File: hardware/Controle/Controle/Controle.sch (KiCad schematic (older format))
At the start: 11 parts

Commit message: PCB
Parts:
- removed C? (x5): 100n, Capacitor_SMD:C_0805_2012Metric_Pad1.18x1.45mm_HandSolder, symbol Device:C_Small
- removed J?: Conn_01x04, symbol Connector_Generic:Conn_01x04
- removed R?: 4k7, symbol Device:R_Small
- removed U?: STM32F103C8Tx, Package_QFP:LQFP-48_7x7mm_P0.5mm, symbol MCU_ST_STM32F1:STM32F103C8Tx
- removed U?: MCP2551-I-SN, Package_SO:SOIC-8_3.9x4.9mm_P1.27mm, symbol Interface_CAN_LIN:MCP2551-I-SN
- removed U?: AZ1117-5.0, symbol Regulator_Linear:AZ1117-5.0
- removed U?: AZ1117-3.3, symbol Regulator_Linear:AZ1117-3.3
- added C101: 100n, Capacitor_SMD:C_0603_1608Metric_Pad1.08x0.95mm_HandSolder, symbol Device:C_Small
- added D101: LL4148, Diode_SMD:D_SOD-523, symbol Device:D_Small
- added F101: 500ma, Fuse:Fuse_0805_2012Metric_Pad1.15x1.40mm_HandSolder, symbol Device:Fuse
- added J101: USART, Connector_PinHeader_2.54mm:PinHeader_1x04_P2.54mm_Vertical, symbol Connector_Generic:Conn_01x04
- added J102: ST_LINK, Connector_PinHeader_2.54mm:PinHeader_1x04_P2.54mm_Vertical, symbol Connector_Generic:Conn_01x04
- added J103: FAN, Connector_PinHeader_2.54mm:PinHeader_1x02_P2.54mm_Vertical, symbol Connector_Generic:Conn_01x02
- added J104: Switches, Connector_PinHeader_1.27mm:PinHeader_2x07_P1.27mm_Vertical_SMD, symbol Connector_Generic:Conn_02x07_Odd_Even
- added Q101: BCV27, Package_TO_SOT_SMD:SOT-23_Handsoldering, symbol Device:Q_NPN_BEC
- added R101, R102: ?, Resistor_SMD:R_0603_1608Metric_Pad0.98x0.95mm_HandSolder, symbol Device:R_Small
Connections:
- net labels added: +15V, +3V3
- net labels removed: CAN_RX, CAN_TX
- wire segments 59 -> 76

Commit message: adicionado o TL7726 e modificada a placa
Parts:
- J101, J102: footprint Connector_PinHeader_2.54mm:PinHeader_1x04_P2.54mm_Vertical -> Connector_PinHeader_2.54mm:PinHeader_1x04_P2.54mm_Vertical_SMD_Pin1Left
- J103: footprint Connector_PinHeader_2.54mm:PinHeader_1x02_P2.54mm_Vertical -> Connector_PinHeader_2.54mm:PinHeader_1x02_P2.54mm_Vertical_SMD_Pin1Left
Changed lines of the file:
@@
 F 0 "J102" H 1468 2317 50  0000 C CNN
 F 1 "ST_LINK" H 1550 2200 50  0000 C CNN
-F 2 "Connector_PinHeader_2.54mm:PinHeader_1x04_P2.54mm_Vertical" H 1550 2000 50  0001 C CNN
+F 2 "Connector_PinHeader_2.54mm:PinHeader_1x04_P2.54mm_Vertical_SMD_Pin1Left" H 1550 2000 50  0001 C CNN
 F 3 "~" H 1550 2000 50  0001 C CNN
 	1    1550 2000
@@
 F 0 "J101" H 1468 1667 50  0000 C CNN
 F 1 "USART" H 1468 1576 50  0000 C CNN
-F 2 "Connector_PinHeader_2.54mm:PinHeader_1x04_P2.54mm_Vertical" H 1550 1350 50  0001 C CNN
+F 2 "Connector_PinHeader_2.54mm:PinHeader_1x04_P2.54mm_Vertical_SMD_Pin1Left" H 1550 1350 50  0001 C CNN
 F 3 "~" H 1550 1350 50  0001 C CNN
 	1    1550 1350
@@
 F 0 "J103" H 1518 2675 50  0000 C CNN
 F 1 "FAN" H 1600 2800 50  0000 C CNN
-F 2 "Connector_PinHeader_2.54mm:PinHeader_1x02_P2.54mm_Vertical" H 1600 3000 50  0001 C CNN
+F 2 "Connector_PinHeader_2.54mm:PinHeader_1x02_P2.54mm_Vertical_SMD_Pin1Left" H 1600 3000 50  0001 C CNN
 F 3 "~" H 1600 3000 50  0001 C CNN
 	1    1600 3000

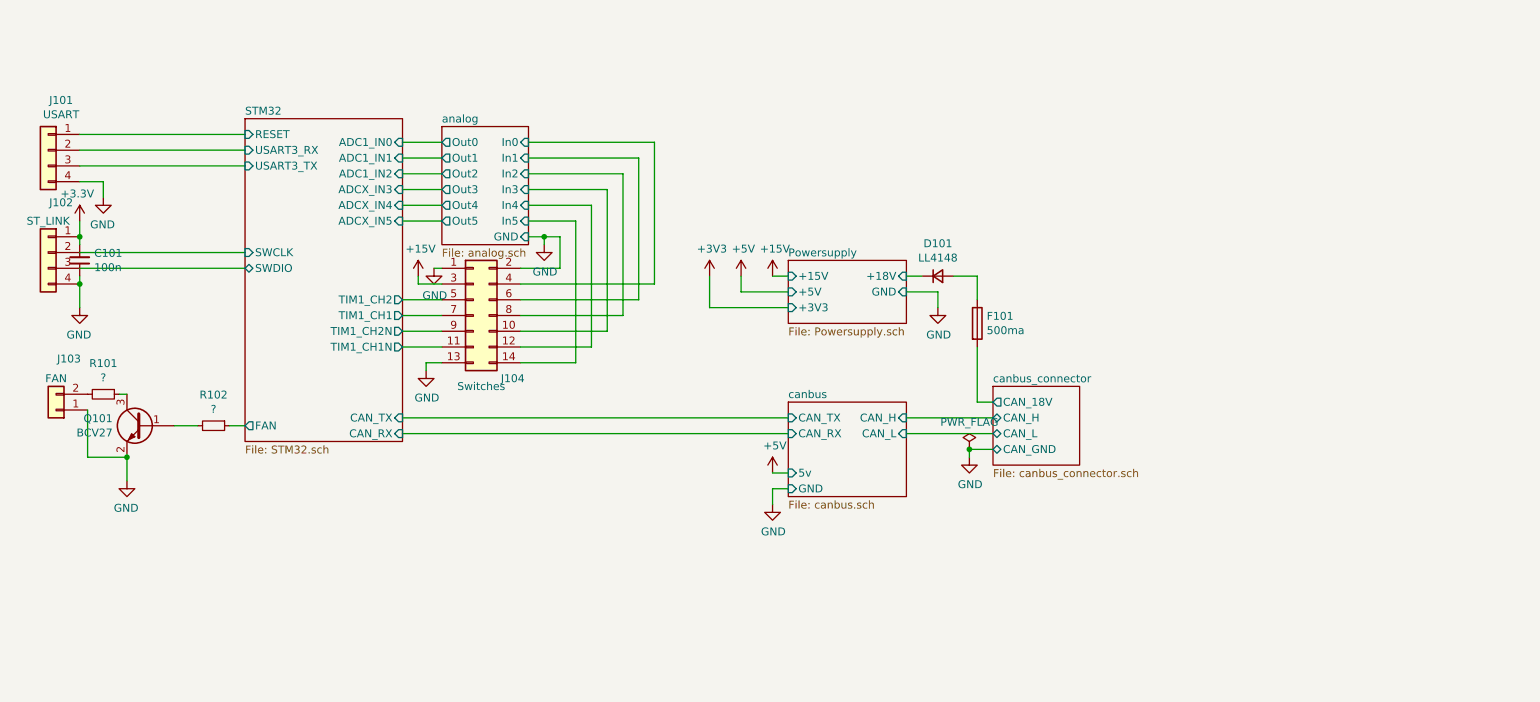
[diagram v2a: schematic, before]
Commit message: control PCB updated
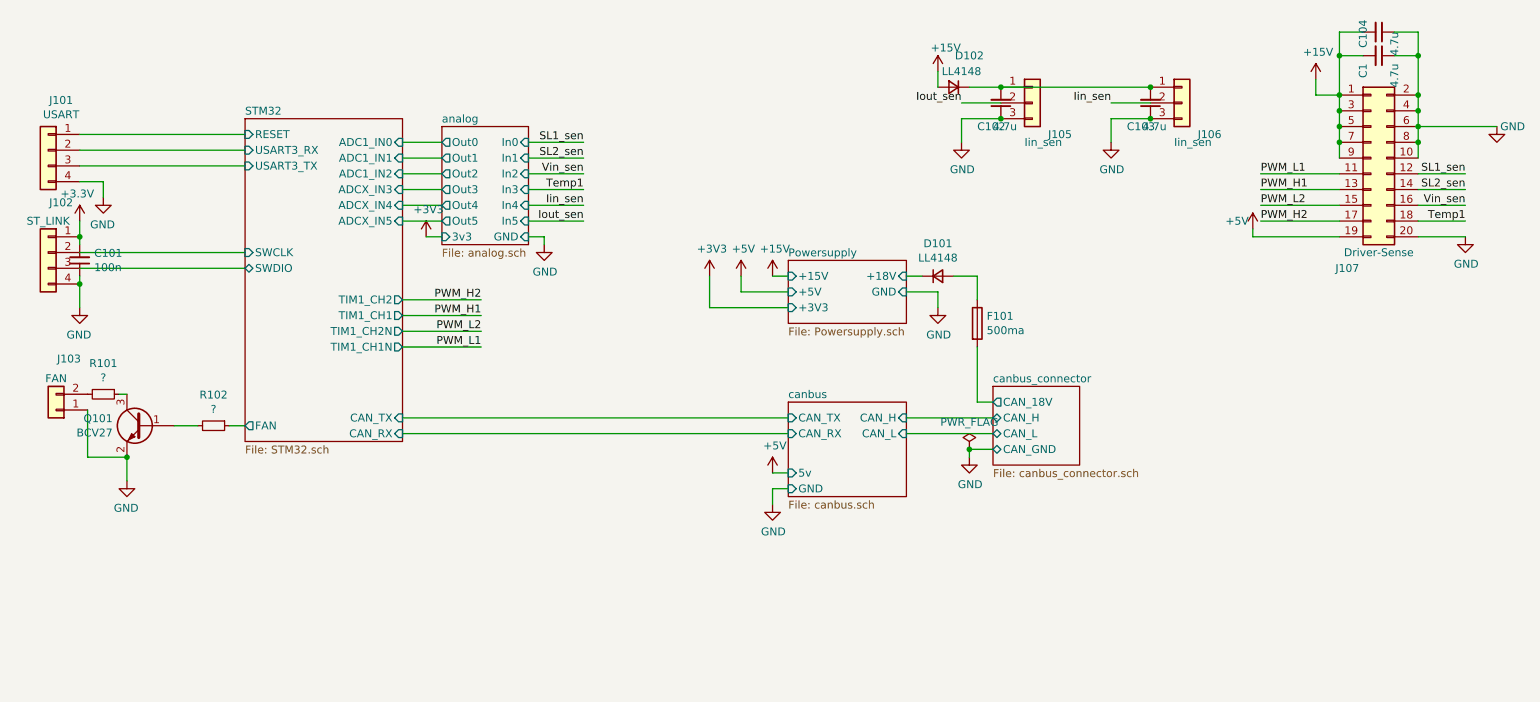
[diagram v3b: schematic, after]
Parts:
- removed J104: Switches, Connector_PinHeader_1.27mm:PinHeader_2x07_P1.27mm_Vertical_SMD, symbol Connector_Generic:Conn_02x07_Odd_Even
- added C1, C102, C103, C104: 4.7u, Capacitor_SMD:C_1210_3225Metric_Pad1.33x2.70mm_HandSolder, symbol Device:C_Small
- added D102: LL4148, Diode_SMD:D_SOD-523, symbol Device:D_Small
- added J105, J106: Iin_sen, Connector_PinHeader_2.54mm:PinHeader_1x03_P2.54mm_Vertical_SMD_Pin1Left, symbol Connector_Generic:Conn_01x03
- added J107: Driver-Sense, KicadZeniteSolarLibrary18:PinSocket_2x10_P1.27mm_Vertical_SMD, symbol Connector_Generic:Conn_02x10_Odd_Even
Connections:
- net +15V: now also C1.2, C104.2, D102.2 (A), J107.1 (Pin_1), J107.3 (Pin_3), J107.5 (Pin_5), J107.7 (Pin_7), J107.9 (Pin_9)
- net +5V: now also J107.19 (Pin_19)
- net GND: now also C1.1, C102.1, C103.1, C104.1, J105.3 (Pin_3), J106.3 (Pin_3), J107.10 (Pin_10), J107.2 (Pin_2), J107.20 (Pin_20), J107.4 (Pin_4), J107.6 (Pin_6), J107.8 (Pin_8)
- new net: C102.2, C103.2, D102.1 (K), J105.1 (Pin_1), J106.1 (Pin_1)
- new net Iin_sen: J106.2 (Pin_2)
- new net Iout_sen: J105.2 (Pin_2)
- new net PWM_H1: J107.13 (Pin_13)
- new net PWM_H2: J107.17 (Pin_17)
- new net PWM_L1: J107.11 (Pin_11)
- new net PWM_L2: J107.15 (Pin_15)
- new net SL1_sen: J107.12 (Pin_12)
- new net SL2_sen: J107.14 (Pin_14)
- new net Temp1: J107.18 (Pin_18)
- new net Vin_sen: J107.16 (Pin_16)

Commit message: Update Controle PCB
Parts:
- D101, D102: value LL4148 -> B0530W; footprint Diode_SMD:D_SOD-523 -> Diode_SMD:D_SOD-123F
- J102: footprint Connector_PinHeader_2.54mm:PinHeader_1x04_P2.54mm_Vertical_SMD_Pin1Left -> Connector_PinHeader_2.54mm:PinHeader_1x05_P2.54mm_Vertical_SMD_Pin1Left; symbol Connector_Generic:Conn_01x04 -> Connector_Generic:Conn_01x05
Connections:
- net GND: now also J102.5 (Pin_5); no longer J102.4 (Pin_4)
- new net STM32/SWO: J102.4 (Pin_4)
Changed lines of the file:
@@
 F18 "SWDIO" B L 2800 2100 50
 F19 "RESET" I L 2800 1250 50
+F20 "SWO" I L 2800 2200 50
 $EndSheet
 $Comp
@@
 Wire Wire Line
 	6150 3400 6250 3400
-$Comp
-L Connector_Generic:Conn_01x04 J102
-U 1 1 6075C4FB
-P 1550 2000
-AR Path="/6075C4FB" Ref="J102"  Part="1"
-AR Path="/607427E0/6075C4FB" Ref="J?"  Part="1"
-F 0 "J102" H 1468 2317 50  0000 C CNN
-F 1 "ST_LINK" H 1550 2200 50  0000 C CNN
-F 2 "Connector_PinHeader_2.54mm:PinHeader_1x04_P2.54mm_Vertical_SMD_Pin1Left" H 1550 2000 50  0001 C CNN
-F 3 "~" H 1550 2000 50  0001 C CNN
-	1    1550 2000
-	-1   0    0    -1
-$EndComp
 $Comp
 L power:GND #PWR0102
@@
 $EndComp
 Wire Wire Line
-	1750 1800 1750 1900
-$Comp
-L Device:C_Small C101
-U 1 1 6075C510
-P 1750 2050
-AR Path="/6075C510" Ref="C101"  Part="1"
-AR Path="/607427E0/6075C510" Ref="C?"  Part="1"
-F 0 "C101" H 1658 2004 50  0000 R CNN
-F 1 "100n" H 1658 2095 50  0000 R CNN
-F 2 "Capacitor_SMD:C_0603_1608Metric_Pad1.08x0.95mm_HandSolder" H 1750 2050 50  0001 C CNN
-F 3 "~" H 1750 2050 50  0001 C CNN
-	1    1750 2050
-	-1   0    0    1
-$EndComp
-Wire Wire Line
-	1750 1950 1750 1900
-Connection ~ 1750 1900
-Wire Wire Line
-	1750 2150 1750 2200
-Connection ~ 1750 2200
-Wire Wire Line
-	1750 2200 1750 2350
-Wire Wire Line
-	1750 2000 2800 2000
-Wire Wire Line
-	1750 2100 2800 2100
+	1700 2100 2800 2100
 $Comp
 L Connector_Generic:Conn_01x04 J101
@@
 Wire Wire Line
 	7450 2300 7450 2150
-$Comp
-L Device:D_Small D101
-U 1 1 6093366B
-P 7200 2150
-F 0 "D101" H 7200 2357 50  0000 C CNN
-F 1 "LL4148" H 7200 2266 50  0000 C CNN
-F 2 "Diode_SMD:D_SOD-523" V 7200 2150 50  0001 C CNN
-F 3 "~" V 7200 2150 50  0001 C CNN
-	1    7200 2150
-	1    0    0    -1
-$EndComp
 Wire Wire Line
 	7100 2150 7000 2150
@@
 P 7300 950
 F 0 "D102" H 7200 750 50  0000 C CNN
-F 1 "LL4148" H 7250 850 50  0000 C CNN
-F 2 "Diode_SMD:D_SOD-523" V 7300 950 50  0001 C CNN
+F 1 "B0530W" H 7050 850 50  0000 C CNN
+F 2 "Diode_SMD:D_SOD-123F" V 7300 950 50  0001 C CNN
 F 3 "~" V 7300 950 50  0001 C CNN
 	1    7300 950
@@
 Wire Wire Line
 	3950 1900 4050 1900
+$Comp
+L Connector_Generic:Conn_01x05 J102
+U 1 1 6075C4FB
+P 1500 2100
+AR Path="/6075C4FB" Ref="J102"  Part="1"
+AR Path="/607427E0/6075C4FB" Ref="J?"  Part="1"
+F 0 "J102" H 1418 2417 50  0000 C CNN
+F 1 "ST_LINK" H 1500 2300 50  0000 C CNN
+F 2 "Connector_PinHeader_2.54mm:PinHeader_1x05_P2.54mm_Vertical_SMD_Pin1Left" H 1500 2100 50  0001 C CNN
+F 3 "~" H 1500 2100 50  0001 C CNN
+	1    1500 2100
+	-1   0    0    -1
+$EndComp
+Wire Wire Line
+	1750 1800 1750 1900
+Wire Wire Line
+	1700 1900 1750 1900
+Connection ~ 1750 1900
+Wire Wire Line
+	1750 2350 1750 2300
+Wire Wire Line
+	1700 2300 1750 2300
+Connection ~ 1750 2300
+Wire Wire Line
+	1750 1900 1750 1950
+Wire Wire Line
+	1700 2000 2800 2000
+Wire Wire Line
+	1750 2300 1750 2150
+Wire Wire Line
+	2800 2200 1700 2200
+$Comp
+L Device:C_Small C101
+U 1 1 6075C510
+P 1750 2050
+AR Path="/6075C510" Ref="C101"  Part="1"
+AR Path="/607427E0/6075C510" Ref="C?"  Part="1"
+F 0 "C101" H 1658 2004 50  0000 R CNN
+F 1 "100n" H 1658 2095 50  0000 R CNN
+F 2 "Capacitor_SMD:C_0603_1608Metric_Pad1.08x0.95mm_HandSolder" H 1750 2050 50  0001 C CNN
+F 3 "~" H 1750 2050 50  0001 C CNN
+	1    1750 2050
+	-1   0    0    1
+$EndComp
+$Comp
+L Device:D_Small D101
+U 1 1 609E3BEA
+P 7200 2150
+F 0 "D101" H 7100 2350 50  0000 C CNN
+F 1 "B0530W" H 7350 2250 50  0000 C CNN
+F 2 "Diode_SMD:D_SOD-123F" V 7200 2150 50  0001 C CNN
+F 3 "~" V 7200 2150 50  0001 C CNN
+	1    7200 2150
+	1    0    0    -1
+$EndComp
 $EndSCHEMATC

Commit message: first version of layout
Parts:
- added H101, H102, H103: MountingHole, MountingHole:MountingHole_3.2mm_M3, symbol Mechanical:MountingHole
- added R103: ?, Resistor_SMD:R_0603_1608Metric_Pad0.98x0.95mm_HandSolder, symbol Device:R_Small
- F101: value 500ma -> 1A; footprint Fuse:Fuse_0805_2012Metric_Pad1.15x1.40mm_HandSolder -> Fuse:Fuse_1812_4532Metric_Pad1.30x3.40mm_HandSolder
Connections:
- net +5V: now also R103.2
- net at J103.2 (Pin_2), R101.2: now also R103.1
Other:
- moved on the sheet: R101
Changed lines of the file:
@@
 L Device:R_Small R101
 U 1 1 60904DF2
-P 1900 2900
-F 0 "R101" V 1704 2900 50  0000 C CNN
-F 1 "?" V 1795 2900 50  0000 C CNN
-F 2 "Resistor_SMD:R_0603_1608Metric_Pad0.98x0.95mm_HandSolder" H 1900 2900 50  0001 C CNN
-F 3 "~" H 1900 2900 50  0001 C CNN
-	1    1900 2900
+P 1950 2900
+F 0 "R101" V 1754 2900 50  0000 C CNN
+F 1 "?" V 1845 2900 50  0000 C CNN
+F 2 "Resistor_SMD:R_0603_1608Metric_Pad0.98x0.95mm_HandSolder" H 1950 2900 50  0001 C CNN
+F 3 "~" H 1950 2900 50  0001 C CNN
+	1    1950 2900
 	0    1    1    0
 $EndComp
-Wire Wire Line
-	2000 2900 2050 2900
 $Comp
 L Device:Fuse F101
@@
 P 7450 2450
 F 0 "F101" H 7510 2496 50  0000 L CNN
-F 1 "500ma" H 7510 2405 50  0000 L CNN
-F 2 "Fuse:Fuse_0805_2012Metric_Pad1.15x1.40mm_HandSolder" V 7380 2450 50  0001 C CNN
+F 1 "1A" H 7510 2405 50  0000 L CNN
+F 2 "Fuse:Fuse_1812_4532Metric_Pad1.30x3.40mm_HandSolder" V 7380 2450 50  0001 C CNN
 F 3 "~" H 7450 2450 50  0001 C CNN
 	1    7450 2450
@@
 	1    0    0    -1
 $EndComp
+$Comp
+L Device:R_Small R103
+U 1 1 60A35BB8
+P 1850 2750
+F 0 "R103" H 1800 2600 50  0000 C CNN
+F 1 "?" H 1650 2600 50  0000 C CNN
+F 2 "Resistor_SMD:R_0603_1608Metric_Pad0.98x0.95mm_HandSolder" H 1850 2750 50  0001 C CNN
+F 3 "~" H 1850 2750 50  0001 C CNN
+	1    1850 2750
+	-1   0    0    1
+$EndComp
+Wire Wire Line
+	1800 2900 1850 2900
+Wire Wire Line
+	1850 2850 1850 2900
+Connection ~ 1850 2900
+$Comp
+L power:+5V #PWR0130
+U 1 1 60A3FB9E
+P 1850 2600
+F 0 "#PWR0130" H 1850 2450 50  0001 C CNN
+F 1 "+5V" H 1865 2773 50  0000 C CNN
+F 2 "" H 1850 2600 50  0001 C CNN
+F 3 "" H 1850 2600 50  0001 C CNN
+	1    1850 2600
+	1    0    0    -1
+$EndComp
+Wire Wire Line
+	1850 2600 1850 2650
+$Comp
+L Mechanical:MountingHole H101
+U 1 1 60AAC1BB
+P 9600 2800
+F 0 "H101" H 9700 2846 50  0000 L CNN
+F 1 "MountingHole" H 9700 2755 50  0000 L CNN
+F 2 "MountingHole:MountingHole_3.2mm_M3" H 9600 2800 50  0001 C CNN
+F 3 "~" H 9600 2800 50  0001 C CNN
+	1    9600 2800
+	1    0    0    -1
+$EndComp
+$Comp
+L Mechanical:MountingHole H102
+U 1 1 60AADB74
+P 9600 3050
+F 0 "H102" H 9700 3096 50  0000 L CNN
+F 1 "MountingHole" H 9700 3005 50  0000 L CNN
+F 2 "MountingHole:MountingHole_3.2mm_M3" H 9600 3050 50  0001 C CNN
+F 3 "~" H 9600 3050 50  0001 C CNN
+	1    9600 3050
+	1    0    0    -1
+$EndComp
+$Comp
+L Mechanical:MountingHole H103
+U 1 1 60AAE00A
+P 9600 3350
+F 0 "H103" H 9700 3396 50  0000 L CNN
+F 1 "MountingHole" H 9700 3305 50  0000 L CNN
+F 2 "MountingHole:MountingHole_3.2mm_M3" H 9600 3350 50  0001 C CNN
+F 3 "~" H 9600 3350 50  0001 C CNN
+	1    9600 3350
+	1    0    0    -1
+$EndComp

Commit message: falta acabamento
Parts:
- added H?: MountingHole, MountingHole:MountingHole_3.2mm_M3, symbol Mechanical:MountingHole
- C1, C102, C103, C104: footprint Capacitor_SMD:C_1210_3225Metric_Pad1.33x2.70mm_HandSolder -> Capacitor_SMD:C_1206_3216Metric_Pad1.33x1.80mm_HandSolder
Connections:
- net STM32/SWCLK: now also J102.4 (Pin_4); no longer J102.2 (Pin_2)
- net STM32/SWDIO: now also J102.2 (Pin_2); no longer J102.3 (Pin_3)
- net STM32/SWO: now also J102.3 (Pin_3); no longer J102.4 (Pin_4)
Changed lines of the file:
@@
 F15 "TIM1_CH1" O R 3800 2400 50
 F16 "TIM1_CH2" O R 3800 2300 50
-F17 "SWCLK" I L 2800 2000 50
-F18 "SWDIO" B L 2800 2100 50
+F17 "SWCLK" I L 2800 2200 50
+F18 "SWDIO" B L 2800 2000 50
 F19 "RESET" I L 2800 1250 50
-F20 "SWO" I L 2800 2200 50
+F20 "SWO" I L 2800 2100 50
 $EndSheet
 $Comp
@@
 F 0 "C1" H 9950 650 50  0000 R CNN
 F 1 "4.7u" H 9950 850 50  0000 R CNN
-F 2 "Capacitor_SMD:C_1210_3225Metric_Pad1.33x2.70mm_HandSolder" H 10000 750 50  0001 C CNN
+F 2 "Capacitor_SMD:C_1206_3216Metric_Pad1.33x1.80mm_HandSolder" H 10000 750 50  0001 C CNN
 F 3 "~" H 10000 750 50  0001 C CNN
 	1    10000 750
@@
 F 0 "C103" H 8700 1200 50  0000 R CNN
 F 1 "4.7u" H 8600 1200 50  0000 R CNN
-F 2 "Capacitor_SMD:C_1210_3225Metric_Pad1.33x2.70mm_HandSolder" H 8550 1050 50  0001 C CNN
+F 2 "Capacitor_SMD:C_1206_3216Metric_Pad1.33x1.80mm_HandSolder" H 8550 1050 50  0001 C CNN
 F 3 "~" H 8550 1050 50  0001 C CNN
 	1    8550 1050
@@
 F 0 "C104" H 10100 500 50  0000 R CNN
 F 1 "4.7u" H 10150 700 50  0000 R CNN
-F 2 "Capacitor_SMD:C_1210_3225Metric_Pad1.33x2.70mm_HandSolder" H 10000 600 50  0001 C CNN
+F 2 "Capacitor_SMD:C_1206_3216Metric_Pad1.33x1.80mm_HandSolder" H 10000 600 50  0001 C CNN
 F 3 "~" H 10000 600 50  0001 C CNN
 	1    10000 600
@@
 F 0 "C102" H 7750 1200 50  0000 R CNN
 F 1 "4.7u" H 7650 1200 50  0000 R CNN
-F 2 "Capacitor_SMD:C_1210_3225Metric_Pad1.33x2.70mm_HandSolder" H 7600 1050 50  0001 C CNN
+F 2 "Capacitor_SMD:C_1206_3216Metric_Pad1.33x1.80mm_HandSolder" H 7600 1050 50  0001 C CNN
 F 3 "~" H 7600 1050 50  0001 C CNN
 	1    7600 1050
@@
 	1    0    0    -1
 $EndComp
+$Comp
+L Mechanical:MountingHole H?
+U 1 1 60B88A3F
+P 9600 3650
+F 0 "H?" H 9700 3696 50  0000 L CNN
+F 1 "MountingHole" H 9700 3605 50  0000 L CNN
+F 2 "MountingHole:MountingHole_3.2mm_M3" H 9600 3650 50  0001 C CNN
+F 3 "~" H 9600 3650 50  0001 C CNN
+	1    9600 3650
+	1    0    0    -1
+$EndComp

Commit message: Controle PCB waiting revision
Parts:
- gave numbers to parts that had none: 1

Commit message: vias
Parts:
- R101, R102: value ? -> 100R
- R103: value ? -> 10k
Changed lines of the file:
@@
 P 2600 3100
 F 0 "R102" V 2404 3100 50  0000 C CNN
-F 1 "?" V 2495 3100 50  0000 C CNN
+F 1 "100R" V 2495 3100 50  0000 C CNN
 F 2 "Resistor_SMD:R_0603_1608Metric_Pad0.98x0.95mm_HandSolder" H 2600 3100 50  0001 C CNN
 F 3 "~" H 2600 3100 50  0001 C CNN
@@
 P 1950 2900
 F 0 "R101" V 1754 2900 50  0000 C CNN
-F 1 "?" V 1845 2900 50  0000 C CNN
+F 1 "100R" V 1845 2900 50  0000 C CNN
 F 2 "Resistor_SMD:R_0603_1608Metric_Pad0.98x0.95mm_HandSolder" H 1950 2900 50  0001 C CNN
 F 3 "~" H 1950 2900 50  0001 C CNN
@@
 P 1850 2750
 F 0 "R103" H 1800 2600 50  0000 C CNN
-F 1 "?" H 1650 2600 50  0000 C CNN
+F 1 "10k" H 1650 2600 50  0000 C CNN
 F 2 "Resistor_SMD:R_0603_1608Metric_Pad0.98x0.95mm_HandSolder" H 1850 2750 50  0001 C CNN
 F 3 "~" H 1850 2750 50  0001 C CNN
